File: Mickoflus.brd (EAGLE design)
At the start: 100 x 100 mm, 41 parts, among them IC1 74HC595D, IC2 74HC595D

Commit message: Added 5V supply (still no stabilizer from battery to 5V).
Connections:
- net +5V: now also SJ3.2
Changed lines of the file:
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@@
 <signal name="+5V">
 <contactref element="IM1" pad="19"/>
+<contactref element="SJ3" pad="2"/>
+<wire x1="18.542" y1="35.56" x2="80.01" y2="15.24" width="0" layer="19" extent="1-1"/>
 </signal>
 </signals>

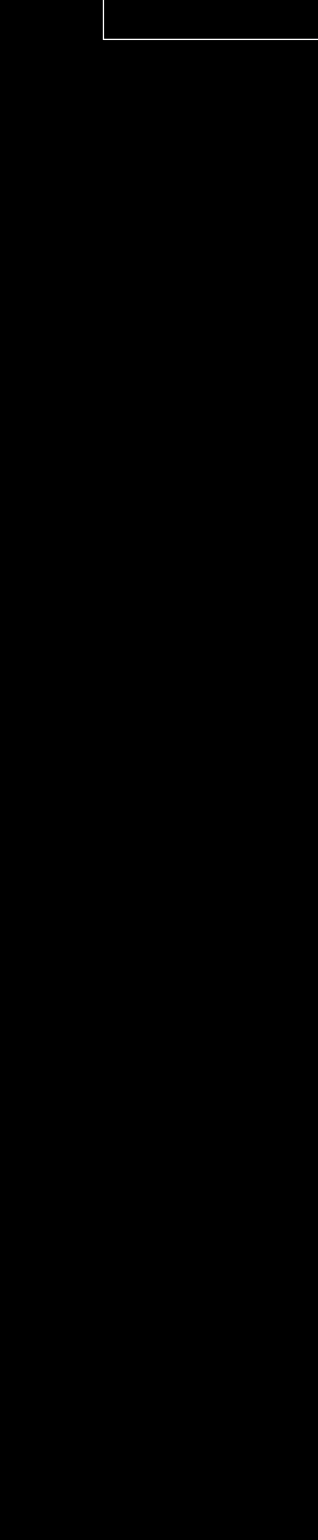
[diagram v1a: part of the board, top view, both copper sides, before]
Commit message: Major schematic improvements changed power supply names: VCC -> +3V3, V+ -> VCC fixed encoder power (+3V3 -> +5V) changed ESP pinout (disconnected internal memory pins, moved encoders out of bootstrap pins) ESP reset also resets motors drivers
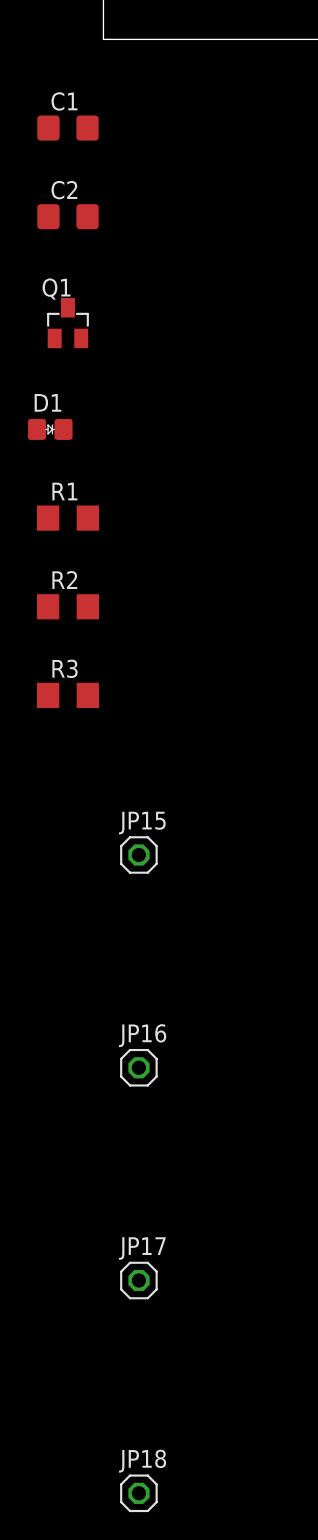
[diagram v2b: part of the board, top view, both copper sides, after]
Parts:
- added C1, C2: 100n, rcl_upravena:C1206
- added D1: (no value), diode:D0805
- added JP15, JP16, JP17, JP18: (no value), pinhead:1X01
- added Q1: (no value), transistors:SOT23
- added R1, R2, R3: 10k, rcl_upravena:R1206
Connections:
- removed net IO10: IM1.17, JP14.7
- removed net IO11: IM1.18, JP14.8
- removed net IO6: IM1.20, JP14.3
- removed net IO7: IM1.21, JP14.4
- removed net IO8: IM1.22, JP14.5
- removed net IO9: IM1.16, JP14.6
- removed net N$104: U$4.ULT
- removed net N$105: U$3.ULT
- removed net N$106: U$2.ULT
- removed net N$107: U$1.ULT
- removed net N$56: IM1.2
- removed net SCLMOT: IC1.10, IC2.10, IM1.30, JP2.2, JP3.5
- removed net V+: POWER1.1, POWER2.1, U$1.VCC, U$2.VCC, U$3.VCC, U$4.VCC
- new net !FAULT0: JP15.1, U$1.ULT
- new net !FAULT1: JP16.1, U$2.ULT
- new net !FAULT2: JP17.1, U$3.ULT
- new net !FAULT3: JP18.1, U$4.ULT
- new net +3V3: C1.1, C2.1, IC1.16, IC2.16, IM1.1, JP2.6, JP3.1, Q1.1, R1.2, R3.2, SJ2.2
- new net EN: IC1.10, IC2.10, IM1.2, JP2.2, JP3.5, Q1.2, R3.1, U$1.!SLEEP, U$2.!SLEEP, U$3.!SLEEP, U$4.!SLEEP
- new net IO10_NC: IM1.17
- new net IO11_NC: IM1.18
- new net IO21: IM1.33
- new net IO6_NC: IM1.20
- new net IO7_NC: IM1.21
- new net IO8_NC: IM1.22
- new net IO9_NC: IM1.16
- new net _EN_: D1.C, Q1.3
- net +5V: now also JP1.4, JP10.4, JP4.4, JP5.4, JP6.4, JP7.4, JP8.4, JP9.4
- net ENC1A: now also IM1.31; no longer IM1.28
- net ENC1B: now also IM1.30; no longer IM1.27
- net ENC2A: now also IM1.29; no longer IM1.26
- net ENC2B: now also IM1.28; no longer IM1.25
- net ENC3A: now also IM1.27; no longer IM1.24
- net ENC3B: now also IM1.26; no longer IM1.23
- net GND: now also C1.2, C2.2, JP1.3, JP10.3, JP2.5, JP3.2, JP4.3, JP5.3, JP6.3, JP7.3, JP8.3, JP9.3, R2.1; no longer JP1.4, JP10.4, JP2.6, JP3.1, JP4.4, JP5.4, JP6.4, JP7.4, JP8.4, JP9.4
- net RCKMOT: now also D1.A, IM1.25, R1.1; no longer IM1.31
- net SCKMOT: now also IM1.23; no longer IM1.29
- net SERMOT: now also IM1.24, R2.2; no longer IM1.33
- net VCC: now also POWER1.1, POWER2.1, U$1.VCC, U$2.VCC, U$3.VCC, U$4.VCC; no longer IC1.16, IC2.16, IM1.1, JP1.3, JP10.3, JP2.5, JP3.2, JP4.3, JP5.3, JP6.3, JP7.3, JP8.3, JP9.3, SJ2.2, U$1.!SLEEP, U$2.!SLEEP, U$3.!SLEEP, U$4.!SLEEP

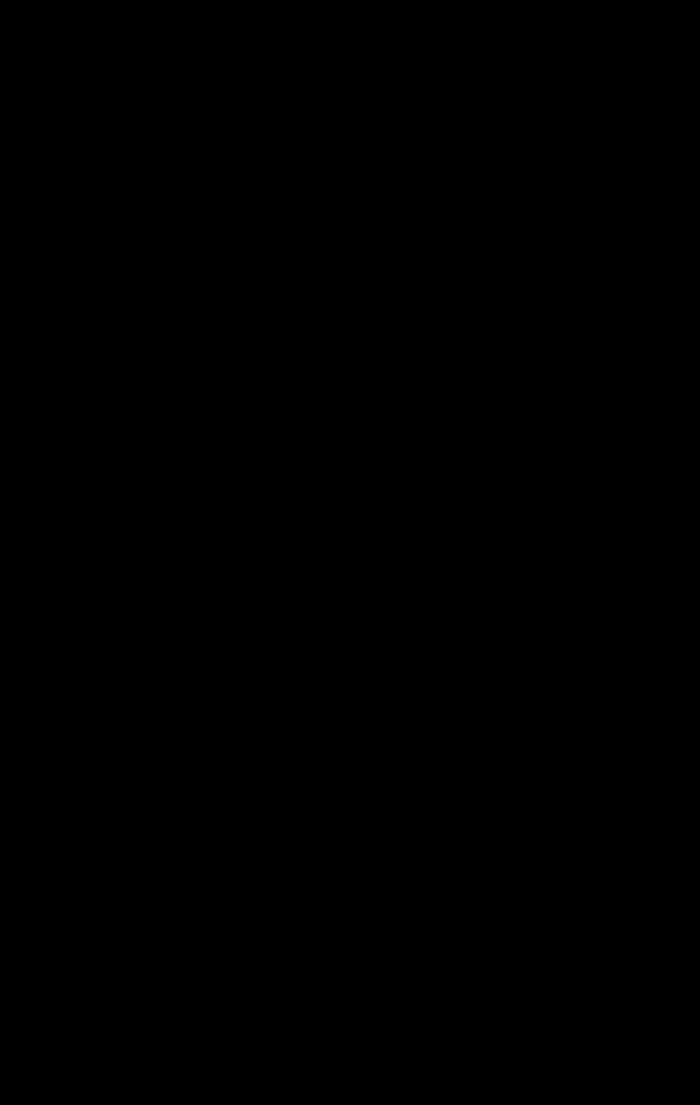
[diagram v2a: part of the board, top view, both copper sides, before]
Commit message: Added voltage regulator and IO expander.
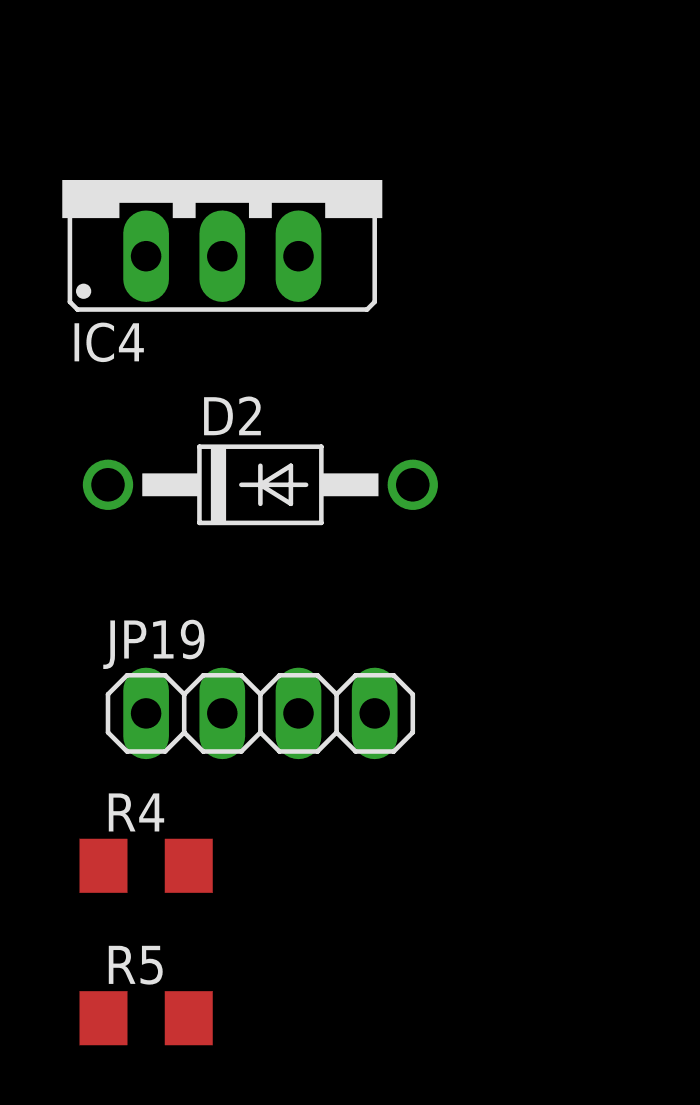
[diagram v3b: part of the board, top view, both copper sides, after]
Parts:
- added D2: 1N4004, diode:DO41-10
- added IC4: (no value), v-reg:78XXS
- added JP19: (no value), pinhead:1X04
- added R4, R5: (no value), resistor:R1206
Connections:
- new net N$5: D2.C, IC4.IN
- new net SCL: IM1.36, JP19.1, R4.1
- new net SDA: IM1.37, JP19.2, R5.1
- net +3V3: now also JP19.3, R4.2, R5.2
- net +5V: now also IC4.OUT
- net GND: now also IC4.GND, JP19.4
- net IO22: no longer IM1.36
- net IO23: no longer IM1.37
- net VCC: now also D2.A
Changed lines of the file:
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@@
 <?xml version="1.0" encoding="utf-8"?>
 <!DOCTYPE eagle SYSTEM "eagle.dtd">
-<eagle version="7.7.0">
+<eagle version="6.5.0">
 <drawing>
 <settings>
@@
 <pass name="Default">
 <param name="RoutingGrid" value="50mil"/>
-<param name="AutoGrid" value="1"/>
-<param name="Efforts" value="0"/>
-<param name="TopRouterVariant" value="1"/>
 <param name="tpViaShape" value="round"/>
 <param name="PrefDir.1" value="|"/>
@@
 <element name="JP17" library="pinhead" package="1X01" value="" x="2.54" y="-88.9"/>
 <element name="JP18" library="pinhead" package="1X01" value="" x="2.54" y="-104.14"/>
+<element name="IC4" library="v-reg" package="78XXS" value="" x="0" y="-114.3"/>
+<element name="D2" library="diode" package="DO41-10" value="1N4004" x="1.27" y="-124.46"/>
+<element name="JP19" library="pinhead" package="1X04" value="" x="1.27" y="-132.08"/>
+<element name="R4" library="resistor" package="R1206" value="" x="-2.54" y="-137.16"/>
+<element name="R5" library="resistor" package="R1206" value="" x="-2.54" y="-142.24"/>
 </elements>
 <signals>
@@
 <contactref element="JP2" pad="5"/>
 <contactref element="R2" pad="1"/>
+<contactref element="IC4" pad="GND"/>
+<contactref element="JP19" pad="4"/>
 <wire x1="133.502" y1="93.98" x2="133.502" y2="107.95" width="0" layer="19" extent="1-1"/>
 <wire x1="133.502" y1="80.01" x2="133.502" y2="93.98" width="0" layer="19" extent="1-1"/>
@@
 <wire x1="-1.14" y1="-12.7" x2="-1.14" y2="-6.35" width="0" layer="19" extent="1-1"/>
 <wire x1="-3.962" y1="-40.64" x2="-1.14" y2="-12.7" width="0" layer="19" extent="1-1"/>
+<wire x1="0" y1="-116.84" x2="-3.962" y2="-40.64" width="0" layer="19" extent="1-1"/>
+<wire x1="5.08" y1="-132.08" x2="0" y2="-116.84" width="0" layer="19" extent="1-1"/>
 </signal>
 <signal name="VCC">
@@
 <contactref element="POWER1" pad="1"/>
 <contactref element="POWER2" pad="1"/>
+<contactref element="D2" pad="A"/>
 <wire x1="77.47" y1="59.69" x2="95.885" y2="91.44" width="0" layer="19" extent="1-1"/>
 <wire x1="58.42" y1="59.69" x2="77.47" y2="59.69" width="0" layer="19" extent="1-1"/>
@@
 <wire x1="19.05" y1="59.69" x2="39.37" y2="59.69" width="0" layer="19" extent="1-1"/>
 <wire x1="3.175" y1="96.52" x2="19.05" y2="59.69" width="0" layer="19" extent="1-1"/>
+<wire x1="6.35" y1="-124.46" x2="19.05" y2="59.69" width="0" layer="19" extent="1-1"/>
 </signal>
 <signal name="N$1">
@@
 </signal>
 <signal name="IO23">
-<contactref element="IM1" pad="37"/>
 <contactref element="JP14" pad="10"/>
-<wire x1="60.96" y1="50.8" x2="36.83" y2="40.64" width="0" layer="19" extent="1-1"/>
 </signal>
 <signal name="IO22">
-<contactref element="IM1" pad="36"/>
 <contactref element="JP14" pad="9"/>
-<wire x1="58.42" y1="50.8" x2="39.37" y2="40.64" width="0" layer="19" extent="1-1"/>
 </signal>
 <signal name="TXD0">
@@
 <contactref element="JP9" pad="4"/>
 <contactref element="JP10" pad="4"/>
+<contactref element="IC4" pad="OUT"/>
 <wire x1="78.74" y1="86.36" x2="88.9" y2="83.82" width="0" layer="19" extent="1-1"/>
 <wire x1="68.58" y1="83.82" x2="78.74" y2="86.36" width="0" layer="19" extent="1-1"/>
@@
 <wire x1="18.542" y1="35.56" x2="27.94" y2="83.82" width="0" layer="19" extent="1-1"/>
 <wire x1="80.01" y1="15.24" x2="18.542" y2="35.56" width="0" layer="19" extent="1-1"/>
+<wire x1="2.54" y1="-116.84" x2="80.01" y2="15.24" width="0" layer="19" extent="1-1"/>
 </signal>
 <signal name="IO9_NC">
@@
 <contactref element="R1" pad="2"/>
 <contactref element="R3" pad="2"/>
+<contactref element="JP19" pad="3"/>
+<contactref element="R4" pad="2"/>
+<contactref element="R5" pad="2"/>
 <wire x1="60.325" y1="71.6534" x2="97.79" y2="73.66" width="0" layer="19" extent="1-1"/>
 <wire x1="27.305" y1="71.6534" x2="60.325" y2="71.6534" width="0" layer="19" extent="1-1"/>
@@
 <wire x1="-1.118" y1="-34.29" x2="-3.49" y2="-21.42" width="0" layer="19" extent="1-1"/>
 <wire x1="-1.118" y1="-46.99" x2="-1.118" y2="-34.29" width="0" layer="19" extent="1-1"/>
+<wire x1="2.54" y1="-132.08" x2="-1.118" y2="-46.99" width="0" layer="19" extent="1-1"/>
+<wire x1="-1.118" y1="-137.16" x2="2.54" y2="-132.08" width="0" layer="19" extent="1-1"/>
+<wire x1="-1.118" y1="-142.24" x2="-1.118" y2="-137.16" width="0" layer="19" extent="1-1"/>
 </signal>
 <signal name="EN">
@@
 <wire x1="2.54" y1="-104.14" x2="72.39" y2="80.01" width="0" layer="19" extent="1-1"/>
 </signal>
+<signal name="N$5">
+<contactref element="D2" pad="C"/>
+<contactref element="IC4" pad="IN"/>
+<wire x1="-2.54" y1="-116.84" x2="-3.81" y2="-124.46" width="0" layer="19" extent="1-1"/>
+</signal>
+<signal name="SDA">
+<contactref element="JP19" pad="2"/>
+<contactref element="IM1" pad="37"/>
+<contactref element="R5" pad="1"/>
+<wire x1="0" y1="-132.08" x2="-3.962" y2="-142.24" width="0" layer="19" extent="1-1"/>
+<wire x1="36.83" y1="40.64" x2="0" y2="-132.08" width="0" layer="19" extent="1-1"/>
+</signal>
+<signal name="SCL">
+<contactref element="JP19" pad="1"/>
+<contactref element="IM1" pad="36"/>
+<contactref element="R4" pad="1"/>
+<wire x1="-2.54" y1="-132.08" x2="-3.962" y2="-137.16" width="0" layer="19" extent="1-1"/>
+<wire x1="39.37" y1="40.64" x2="-2.54" y2="-132.08" width="0" layer="19" extent="1-1"/>
+</signal>
 </signals>
